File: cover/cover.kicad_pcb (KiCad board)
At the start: 2 copper layers, 30.9 x 58.1 mm, 3 parts

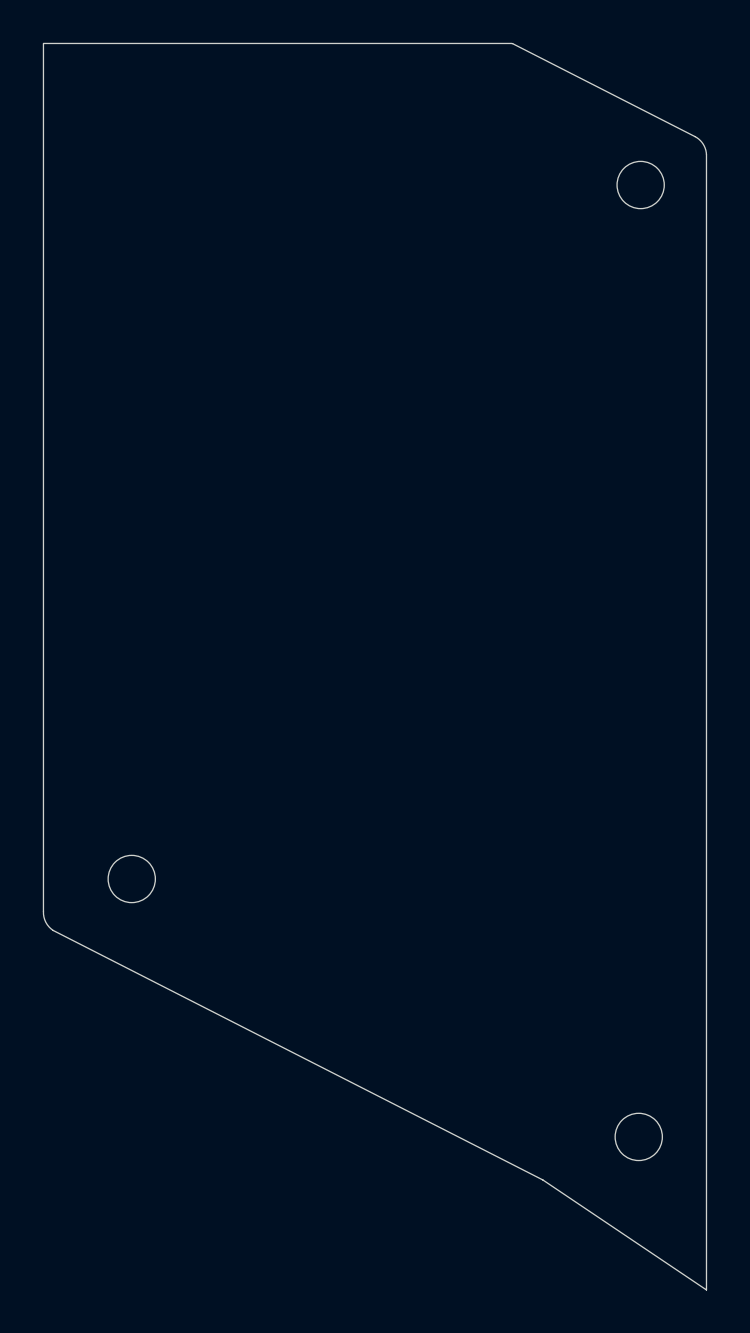
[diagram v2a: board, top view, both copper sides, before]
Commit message: Created a top cover for v4.0
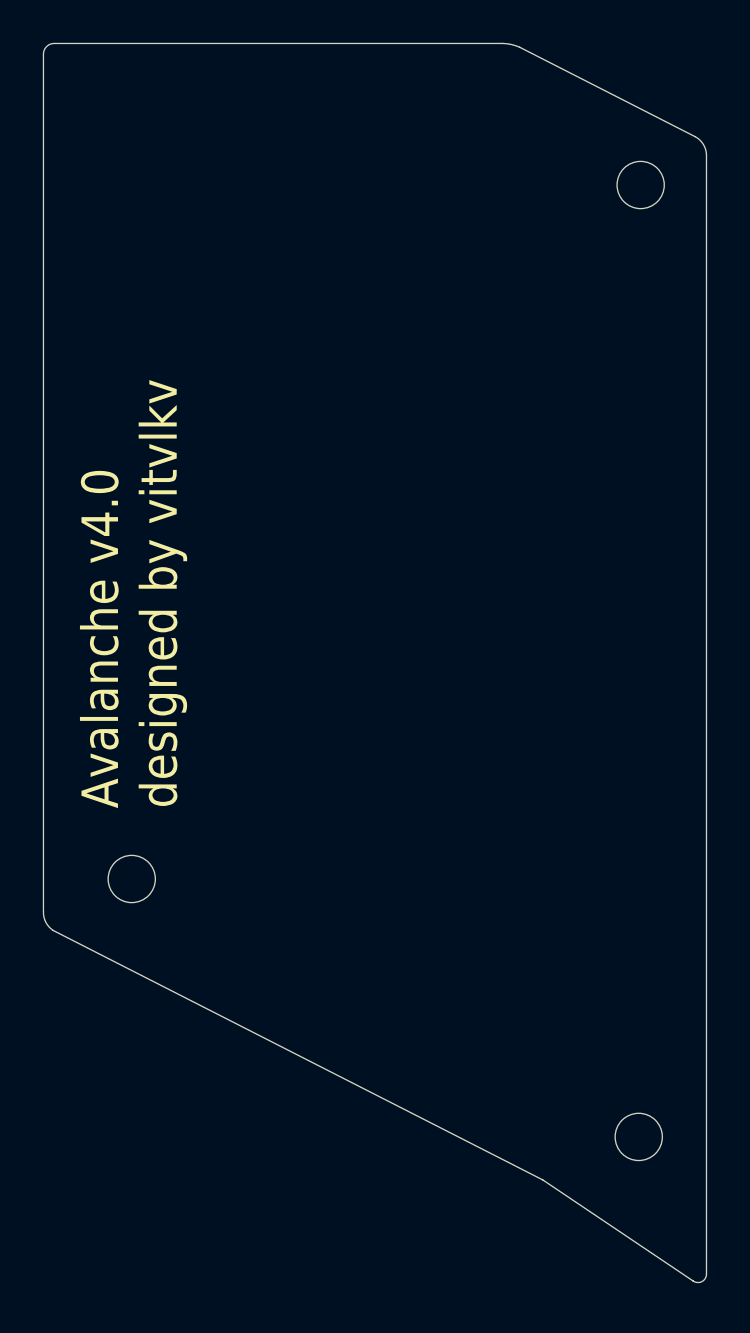
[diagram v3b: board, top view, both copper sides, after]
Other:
- board size 30.9 x 58.1 mm -> 30.9 x 57.7 mm
- board text added: "Avalanche v4.0 designed by vitvlkv"
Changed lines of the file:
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@@
   (general
     (thickness 1.6)
-    (drawings 13)
+    (drawings 18)
     (tracks 0)
     (zones 0)
@@
     (visible_elements FFFFFF7F)
     (pcbplotparams
-      (layerselection 0x010cc_7ffffffe)
+      (layerselection 0x010fc_7ffffffe)
       (usegerberextensions false)
       (usegerberattributes true)
@@
       (drillshape 0)
       (scaleselection 1)
-      (outputdirectory ""))
+      (outputdirectory "Gerbers"))
   )
   (net 0 "")
@@
     (pad "" np_thru_hole circle (at 0 0 340.5) (size 2.2 2.2) (drill 2.2) (layers *.Cu *.Mask))
   )
-  (gr_line (start 199.96 39.665044) (end 199.947878 39.68) (layer Edge.Cuts) (width 0.05))
+  (gr_line (start 221.359976 39.664909) (end 221.29 39.66504) (layer Edge.Cuts) (width 0.05))
+  (gr_line (start 222.13924 39.84149) (end 230.309896 44.005835) (layer Edge.Cuts) (width 0.05))
+  (gr_arc (start 221.300031 41.73721) (end 222.13924 39.84149) (angle -22.22139906) (layer Edge.Cuts) (width 0.05))
+  (gr_arc (start 200.447977 40.165143) (end 200.447977 39.665044) (angle -90) (layer Edge.Cuts) (width 0.05))
+  (gr_line (start 230.209607 97.320142) (end 230.202362 97.316486) (layer Edge.Cuts) (width 0.05))
+  (gr_arc (start 230.448574 97.007218) (end 230.209607 97.320142) (angle -128.4178767) (layer Edge.Cuts) (width 0.05))
+  (gr_text "Avalanche v4.0\ndesigned by vitvlkv" (at 204.00185 75.310403 90) (layer F.SilkS)
+    (effects (font (size 1.7 1.5) (thickness 0.3)) (justify left))
+  )
+  (gr_text "Avalanche v4.0\ndesigned by vitvlkv" (at 204.001845 52.110401 90) (layer B.SilkS)
+    (effects (font (size 1.7 1.5) (thickness 0.3)) (justify left mirror))
+  )
   (gr_line (start 200.074958 80.160872) (end 252.19884 106.719313) (layer Cmts.User) (width 0.15))
   (gr_line (start 200.77496 81.560868) (end 201.074961 59.060882) (layer Cmts.User) (width 0.15))
   (gr_arc (start 200.950259 80.154978) (end 199.94788 80.113509) (angle -59.3) (layer Edge.Cuts) (width 0.05))
-  (gr_line (start 223.218253 92.621212) (end 230.842242 97.746664) (layer Edge.Cuts) (width 0.05))
+  (gr_line (start 223.218253 92.621212) (end 230.202362 97.316486) (layer Edge.Cuts) (width 0.05))
   (gr_circle (center 212.72 58.36) (end 212.844683 58.531638) (layer Cmts.User) (width 0.15))
   (gr_arc (start 229.846502 44.887434) (end 230.841843 44.852134) (angle -60.24128881) (layer Edge.Cuts) (width 0.05))
-  (gr_line (start 221.806128 39.671713) (end 230.309896 44.005835) (layer Edge.Cuts) (width 0.05))
   (gr_line (start 200.40354 80.996157) (end 223.218253 92.621212) (layer Edge.Cuts) (width 0.05))
-  (gr_line (start 221.737224 39.66504) (end 199.96 39.665044) (layer Edge.Cuts) (width 0.05))
-  (gr_line (start 199.94788 80.113509) (end 199.947878 39.68) (layer Edge.Cuts) (width 0.05))
-  (gr_line (start 221.737224 39.66504) (end 221.806128 39.671713) (layer Edge.Cuts) (width 0.05))
-  (gr_line (start 230.841843 44.852134) (end 230.842242 97.746664) (layer Edge.Cuts) (width 0.05))
+  (gr_line (start 221.29 39.66504) (end 200.447977 39.665044) (layer Edge.Cuts) (width 0.05))
+  (gr_line (start 199.94788 80.113509) (end 199.947878 40.165143) (layer Edge.Cuts) (width 0.05))
+  (gr_line (start 230.841843 44.852134) (end 230.842242 97) (layer Edge.Cuts) (width 0.05))
 )
